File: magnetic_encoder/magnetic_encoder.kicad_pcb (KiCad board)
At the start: 2 copper layers, 47 x 28.5 mm, 14 parts, among them IC1 AS5311-ATST, J1 Conn_01x07, J11 Conn_01x01, J12 Conn_01x01, J13 Conn_01x01, J17 Conn_01x01, J2 Conn_01x07

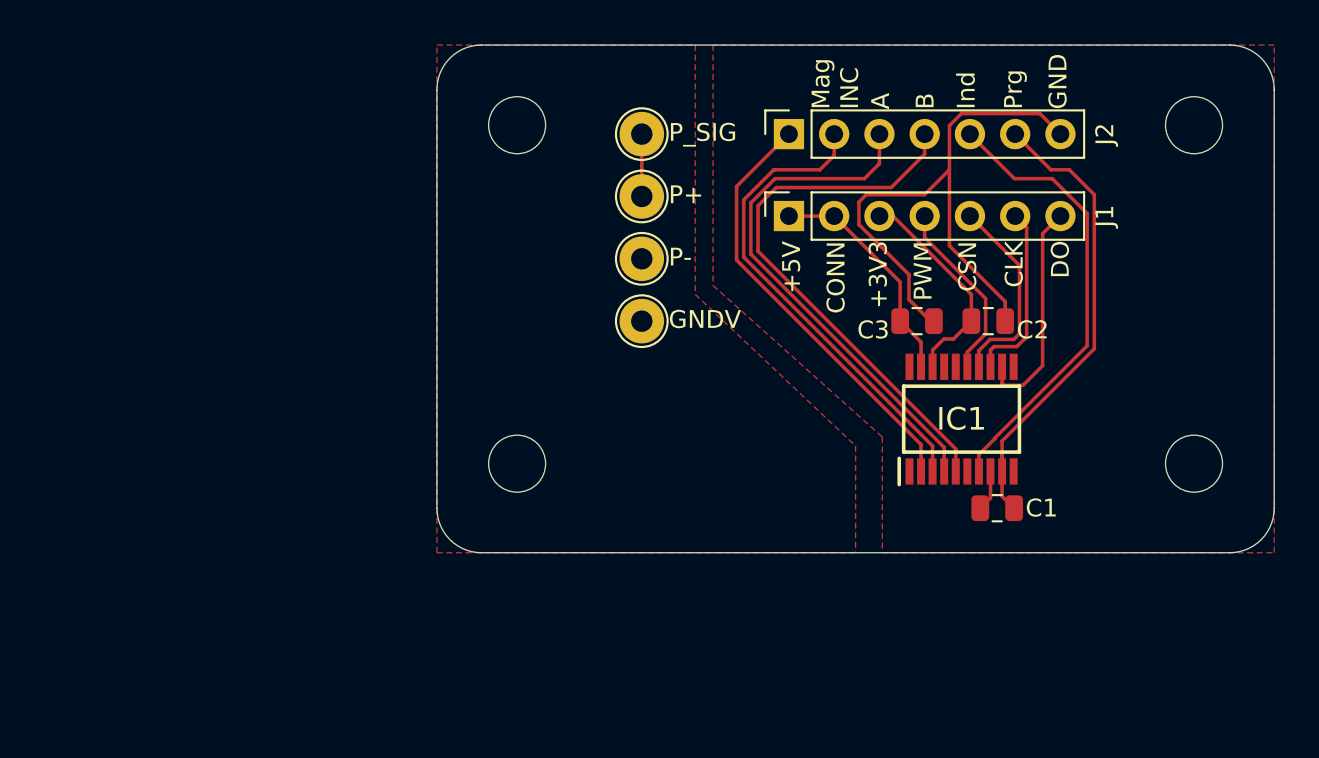
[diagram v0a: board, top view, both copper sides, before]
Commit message: updated unused pins into testpoints
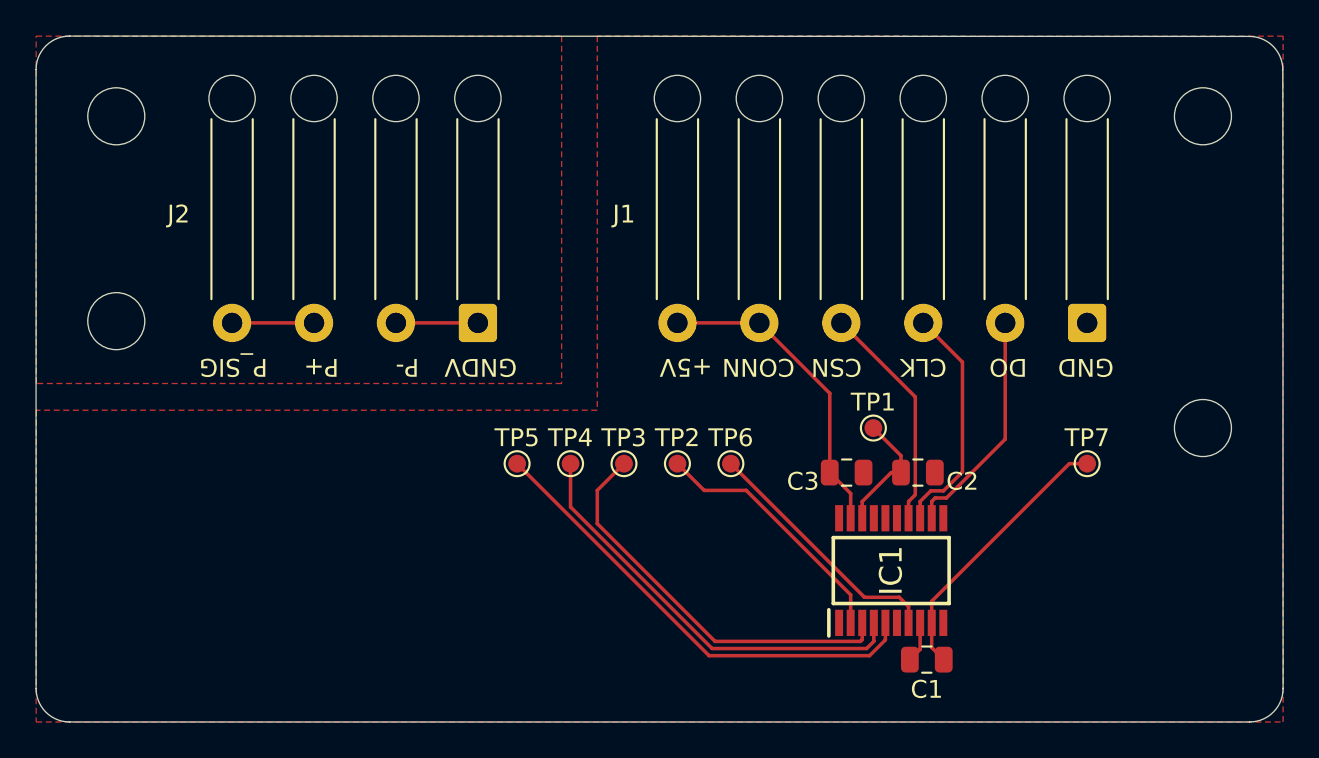
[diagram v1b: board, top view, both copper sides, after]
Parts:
- removed the H2 at (90.0, 49.0)
- removed J11, J12, J13, J17: Conn_01x01, TestPoint:TestPoint_THTPad_D2.5mm_Drill1.2mm
- added H4: MountingHole, MountingHole:MountingHole_3.2mm_M3, F.Cu at (67.5, 41.0)
- added TP1: TestPoint, TestPoint:TestPoint_Pad_D1.0mm, F.Cu at (110.0, 47.0)
- added TP2: TestPoint, TestPoint:TestPoint_Pad_D1.0mm, F.Cu at (99.0, 49.0)
- added TP3: TestPoint, TestPoint:TestPoint_Pad_D1.0mm, F.Cu at (96.0, 49.0)
- added TP4: TestPoint, TestPoint:TestPoint_Pad_D1.0mm, F.Cu at (93.0, 49.0)
- added TP5: TestPoint, TestPoint:TestPoint_Pad_D1.0mm, F.Cu at (90.0, 49.0)
- added TP6: TestPoint, TestPoint:TestPoint_Pad_D1.0mm, F.Cu at (102.0, 49.0)
- added TP7: TestPoint, TestPoint:TestPoint_Pad_D1.0mm, F.Cu at (122.0, 49.0)
- C1: value 100n -> 100n/10V
- C3: value 10u/10V -> 100n/10V
- J1: value Conn_01x07 -> Conn_01x06; footprint Connector_PinSocket_2.54mm:PinSocket_1x07_P2.54mm_Vertical -> Connector_Wire:SolderWire-0.5sqmm_1x06_P4.6mm_D0.9mm_OD2.1mm_Relief
- J2: value Conn_01x07 -> Conn_01x04; footprint Connector_PinSocket_2.54mm:PinSocket_1x07_P2.54mm_Vertical -> Connector_Wire:SolderWire-0.5sqmm_1x04_P4.6mm_D0.9mm_OD2.1mm_Relief
- moved H1 22.5 mm to (67.5, 29.5)
- moved J2 20.4 mm to (87.8, 41.1), turned to 180 degrees
- moved J1 17.8 mm to (122.0, 41.1), turned to 180 degrees
- moved C1 9.37 mm to (113.0, 60.0)
- moved C2 9.37 mm to (112.5, 49.5)
- moved C3 9.37 mm to (108.5, 49.5)
- moved IC1 9.37 mm to (111.0, 55.0)
- moved H3 2.06 mm to (128.5, 47.0)
- moved H2 0.71 mm to (128.5, 29.5)
- renumbered H3 to H2, H4 to H3
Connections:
- J1 pad 1: +5V -> GND
- J1 pad 2: +5V -> /DO
- J1 pad 3: +3.3V -> /CLK
- J1 pad 4: /PWM -> /CSn
- J1 pad 5: /CSn -> +5V
- J1 pad 6: /CLK -> +5V
- J2 pad 1: /MagINC -> /PIEZO_CHx_PA
- J2 pad 2: /MagDEC -> /PIEZO_CHx_PA
- J2 pad 3: /A -> GNDV
- J2 pad 4: /B -> GNDV
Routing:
- net GND: track 35.9 -> 2.49 mm
- net /Prog: track 26.8 -> 15.5 mm
- net /Ind: track 25.4 -> 14.2 mm
- net /PWM: track 10.3 -> 0.00 mm
- net /MagINC: track 24.4 -> 14.4 mm
- net /A: track 29.4 -> 24.0 mm
- net +3.3V: track 12.3 -> 6.93 mm
- net /B: track 31.2 -> 26.5 mm
- net +5V: track 13.0 -> 17.7 mm
- net GNDV: track 0.00 -> 4.60 mm
- net /MagDEC: track 27.0 -> 22.6 mm
- net /CLK: track 10.3 -> 13.3 mm
- net /CSn: track 11.3 -> 12.8 mm
- net /PIEZO_CHx_PA: track 3.50 -> 4.60 mm
- net /DO: track 12.5 -> 13.0 mm
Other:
- board size 47 x 28.5 mm -> 70 x 38.5 mm
- board text removed: "+3V3"
- board text removed: "A"
- board text removed: "B"
- board text removed: "Ind"
- board text removed: "Mag INC"
- board text removed: "PWM"
- board text removed: "Prg"
